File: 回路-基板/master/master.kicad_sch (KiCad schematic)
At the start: 28 parts, among them J1 Ext. PWR, J2 Conn_01x07_Pin, SW1 SW_SPDT, SW2 SW_SPDT, SW3 SW_SPDT, SW4 RESET, U1 TWE-L-DP-W, U2 LM1117MP-3.3, U3 DEV-16771

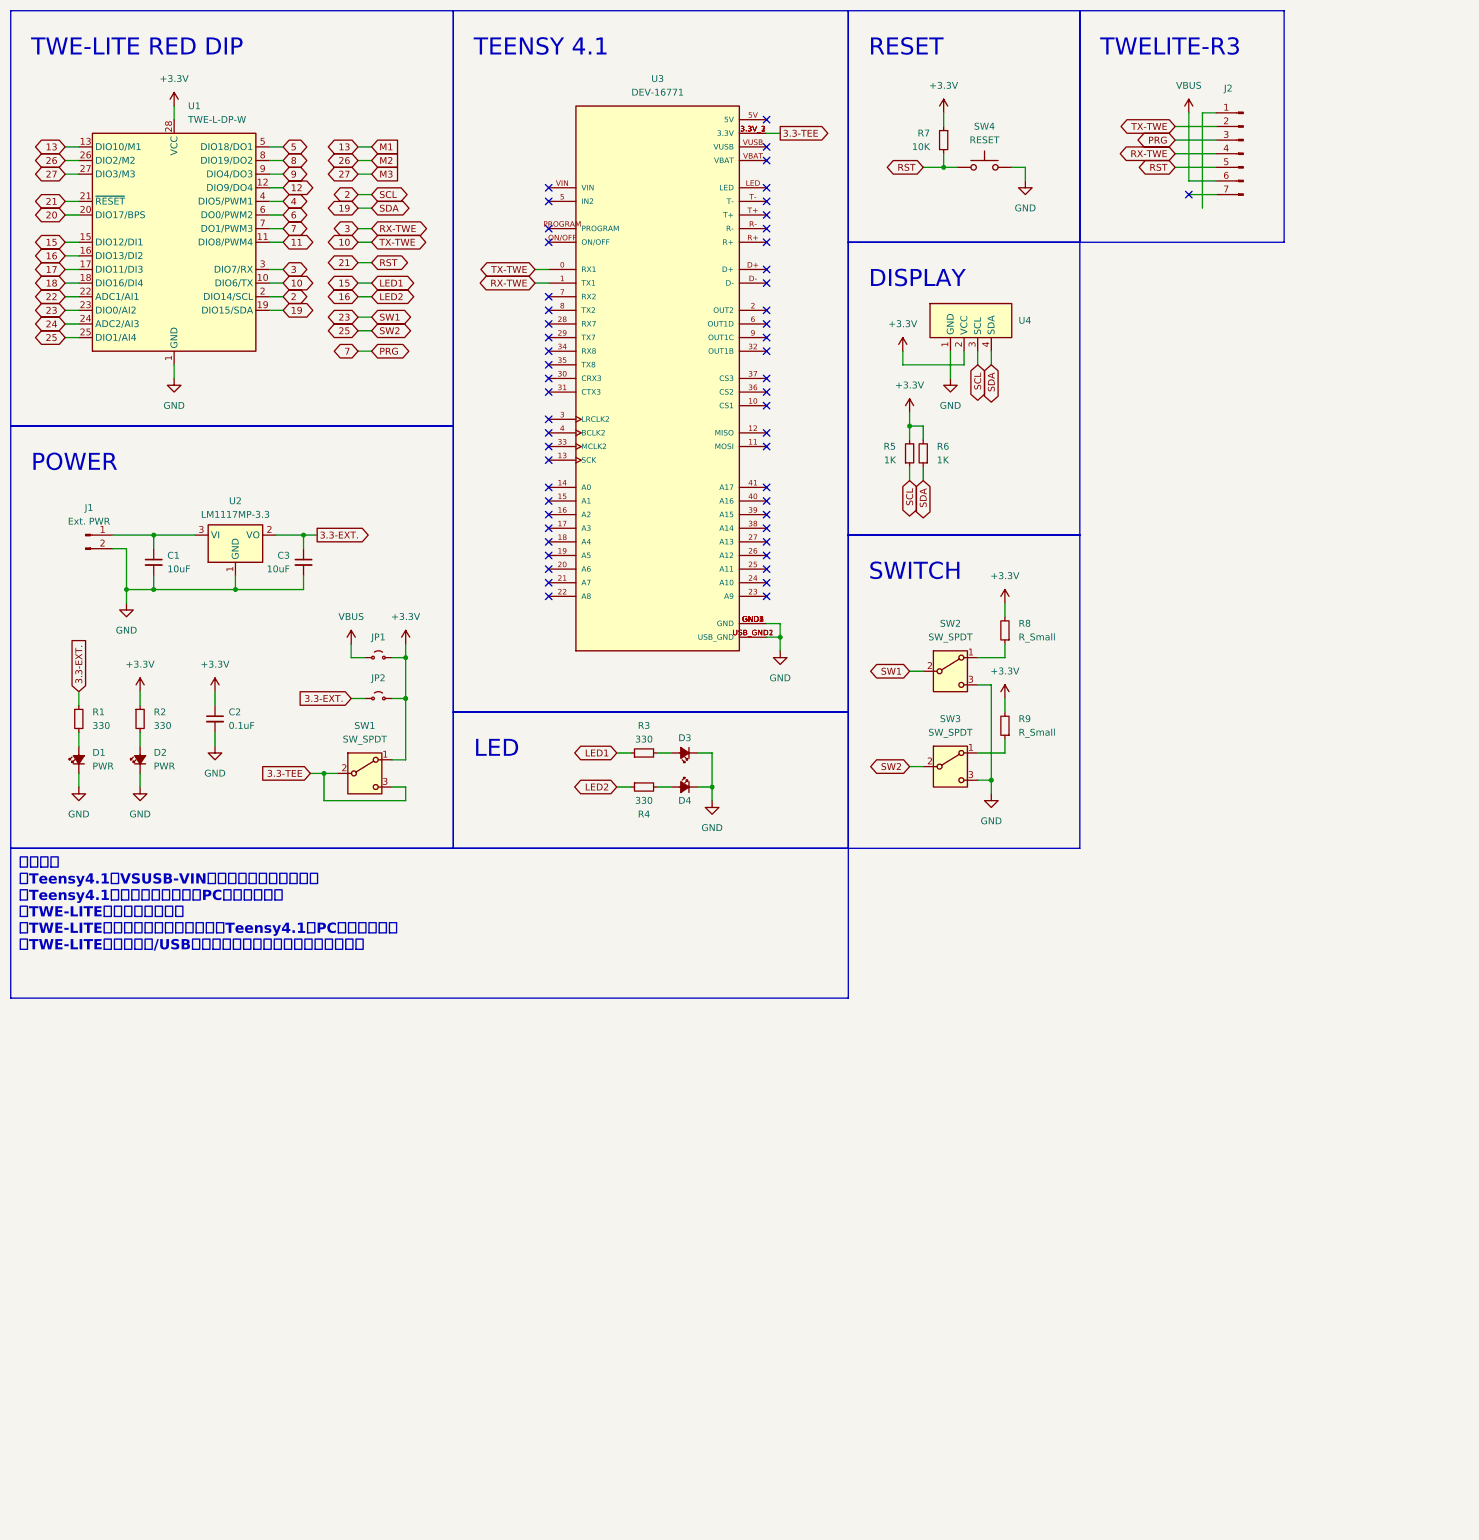
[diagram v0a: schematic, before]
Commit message: 親機基板のPCBを少し進めた
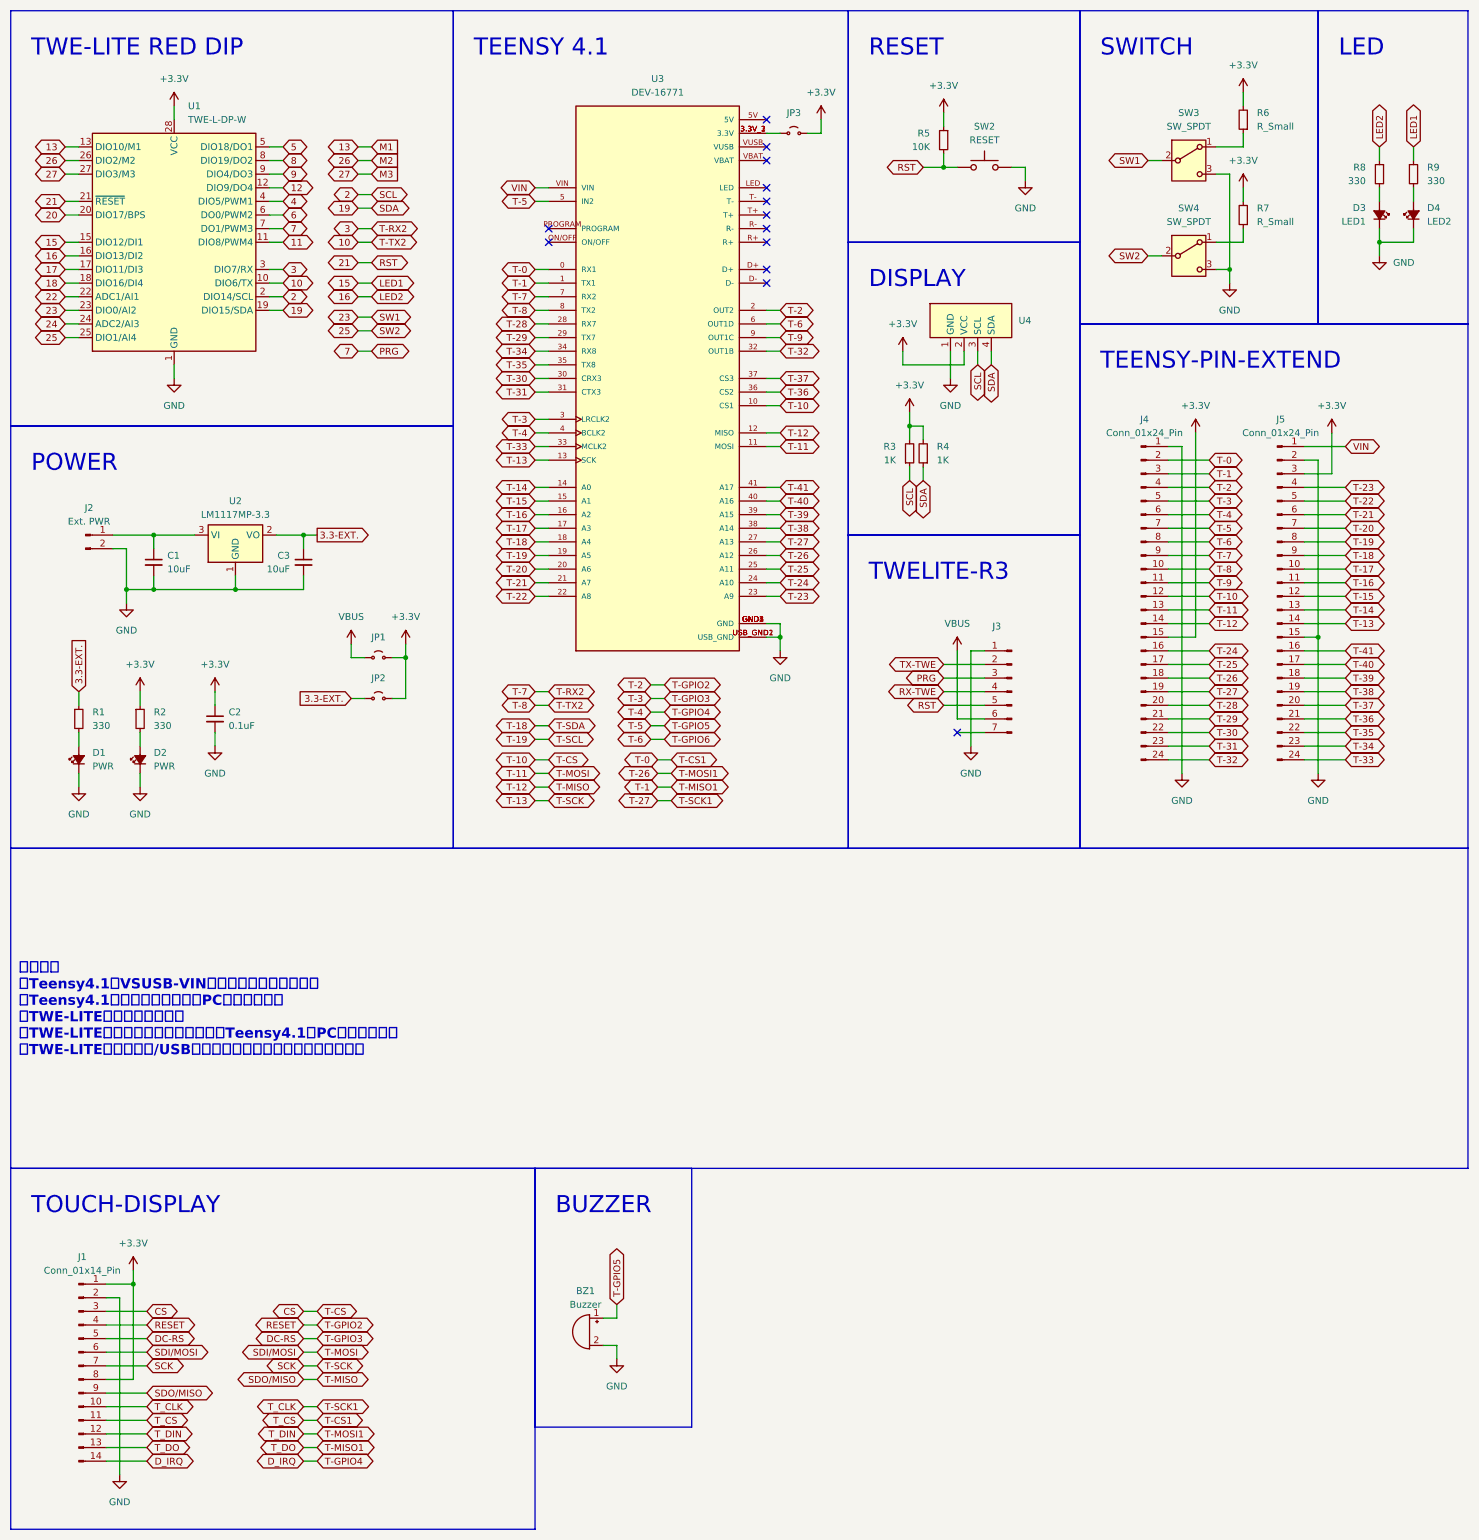
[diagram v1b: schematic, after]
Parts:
- removed R3, R4: 330, symbol Device:R_Small
- removed SW1: SW_SPDT, symbol Switch:SW_SPDT
- added BZ1: Buzzer, @2024-cansat:PKM13EPYH4000-A0, symbol Device:Buzzer
- added J1: Conn_01x14_Pin, Connector_PinSocket_2.54mm:PinSocket_1x14_P2.54mm_Vertical, symbol Connector:Conn_01x14_Pin
- added J4, J5: Conn_01x24_Pin, Connector_PinSocket_2.54mm:PinSocket_1x24_P2.54mm_Vertical, symbol Connector:Conn_01x24_Pin
- added JP3: Jumper_2_Small_Open, Jumper:SolderJumper-2_P1.3mm_Open_Pad1.0x1.5mm, symbol Jumper:Jumper_2_Small_Open
- added R8, R9: 330, Resistor_SMD:R_0603_1608Metric, symbol Device:R_Small
- C1, C2, C3: footprint (none) -> Capacitor_SMD:C_0603_1608Metric
- D1, D2, D3, D4: footprint (none) -> LED_SMD:LED_0805_2012Metric
- J2: renamed from J1; footprint (none) -> Connector_PinHeader_2.54mm:PinHeader_1x02_P2.54mm_Vertical
- J3: renamed from J2; footprint (none) -> Connector_PinSocket_2.54mm:PinSocket_1x07_P2.54mm_Vertical
- JP1, JP2: footprint (none) -> Jumper:SolderJumper-2_P1.3mm_Open_Pad1.0x1.5mm
- R1, R2: footprint (none) -> Resistor_SMD:R_0603_1608Metric
- R3: renamed from R5; footprint (none) -> Resistor_SMD:R_0603_1608Metric
- R4: renamed from R6; footprint (none) -> Resistor_SMD:R_0603_1608Metric
- R5: renamed from R7; footprint (none) -> Resistor_SMD:R_0603_1608Metric
- R6: renamed from R8; footprint (none) -> Resistor_SMD:R_0603_1608Metric
- R7: renamed from R9; footprint (none) -> Resistor_SMD:R_0603_1608Metric
- SW2: renamed from SW4; footprint (none) -> @2024-cansat:Tactile1
- SW3: renamed from SW2; footprint (none) -> @2024-cansat:SS12D01G4
- SW4: renamed from SW3; footprint (none) -> @2024-cansat:SS12D01G4
- U3: footprint DEV-16771:MODULE_DEV-16771 -> @2024-cansat:MODULE_DEV-16771
- U4: footprint (none) -> @2024-cansat:Display
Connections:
- net +3.3V: now also J1.1 (Pin_1), J1.8 (Pin_8), J4.15 (Pin_15), J5.3 (Pin_3), JP3.2 (B)
- net 10: now also U3.8 (TX2), J4.10 (Pin_10); no longer J3.2 (Pin_2), U3.0 (RX1)
- net 15: now also R9.1
- net 16: now also R8.1
- net 3: now also U3.7 (RX2), J4.9 (Pin_9); no longer J3.4 (Pin_4), U3.1 (TX1)
- net GND: now also J3.1 (Pin_1), BZ1.2 (-), J1.2 (Pin_2), J4.1 (Pin_1), J5.15 (Pin_15), J5.2 (Pin_2)
- net at D3.2 (A): now also R8.2
- net CS: now reaches U3.10 (CS1)
- net CS: now also J1.3 (Pin_3), J4.12 (Pin_12)
- net SDI/MOSI: now reaches U3.11 (MOSI)
- net SDI/MOSI: now also J1.6 (Pin_6), J4.13 (Pin_13)
- net SDO/MISO: now reaches U3.12 (MISO)
- net SDO/MISO: now also J1.9 (Pin_9), J4.14 (Pin_14)
- net SCK: now reaches U3.13 (SCK)
- net SCK: now also J1.7 (Pin_7), J5.14 (Pin_14)
- net T-14: now reaches U3.14 (A0)
- net T-14: now also J5.13 (Pin_13)
- net T-15: now reaches U3.15 (A1)
- net T-15: now also J5.12 (Pin_12)
- net T-16: now reaches U3.16 (A2)
- net T-16: now also J5.11 (Pin_11)
- net T-17: now reaches U3.17 (A3)
- net T-17: now also J5.10 (Pin_10)
- net T-18: now reaches U3.18 (A4)
- net T-18: now also J5.9 (Pin_9)
- net T-19: now reaches U3.19 (A5)
- net T-19: now also J5.8 (Pin_8)
- net RESET: now reaches U3.2 (OUT2)
- net RESET: now also J1.4 (Pin_4), J4.4 (Pin_4)
- net T-20: now reaches U3.20 (A6)
- net T-20: now also J5.7 (Pin_7)
- net T-21: now reaches U3.21 (A7)
- net T-21: now also J5.6 (Pin_6)
- net T-22: now reaches U3.22 (A8)
- net T-22: now also J5.5 (Pin_5)
- net T-23: now reaches U3.23 (A9)
- net T-23: now also J5.4 (Pin_4)
- net T-24: now reaches U3.24 (A10)
- net T-24: now also J4.16 (Pin_16)
- net T-25: now reaches U3.25 (A11)
- net T-25: now also J4.17 (Pin_17)
- net T-26: now reaches U3.26 (A12)
- net T-26: now also J1.12 (Pin_12), J4.18 (Pin_18)
- net T-27: now reaches U3.27 (A13)
- net T-27: now also J1.10 (Pin_10), J4.19 (Pin_19)
- net T-28: now reaches U3.28 (RX7)
- net T-28: now also J4.20 (Pin_20)
- net T-29: now reaches U3.29 (TX7)
- net T-29: now also J4.21 (Pin_21)
- net DC-RS: now reaches U3.3 (LRCLK2)
- net DC-RS: now also J1.5 (Pin_5), J4.5 (Pin_5)
- net T-30: now reaches U3.30 (CRX3)
- net T-30: now also J4.22 (Pin_22)
- net T-31: now reaches U3.31 (CTX3)
- net T-31: now also J4.23 (Pin_23)
- net T-32: now reaches U3.32 (OUT1B)
- net T-32: now also J4.24 (Pin_24)
- net T-33: now reaches U3.33 (MCLK2)
- net T-33: now also J5.24 (Pin_24)
- net T-34: now reaches U3.34 (RX8)
- net T-34: now also J5.23 (Pin_23)
- net T-35: now reaches U3.35 (TX8)
- net T-35: now also J5.22 (Pin_22)
- net T-36: now reaches U3.36 (CS2)
- net T-36: now also J5.21 (Pin_21)
- net T-37: now reaches U3.37 (CS3)
- net T-37: now also J5.20 (Pin_20)
- net T-38: now reaches U3.38 (A14)
- net T-38: now also J5.19 (Pin_19)
- net T-39: now reaches U3.39 (A15)
- net T-39: now also J5.18 (Pin_18)
- net D_IRQ: now reaches U3.4 (BCLK2)
- net D_IRQ: now also J1.14 (Pin_14), J4.6 (Pin_6)
- net T-40: now reaches U3.40 (A16)
- net T-40: now also J5.17 (Pin_17)
- net T-41: now reaches U3.41 (A17)
- net T-41: now also J5.16 (Pin_16)
- net T-5: now reaches U3.5 (IN2)
- net T-5: now also BZ1.1 (+), J4.7 (Pin_7)
- net T-6: now reaches U3.6 (OUT1D)
- net T-6: now also J4.8 (Pin_8)
- net T-9: now reaches U3.9 (OUT1C)
- net T-9: now also J4.11 (Pin_11)
- net VIN: now reaches U3.VIN
- net VIN: now also J5.1 (Pin_1)
- net at D4.2 (A): now also R9.2
- net 3.3-TEE: no longer names the net of U3.3.3V_1 (3.3V), U3.3.3V_2 (3.3V), U3.3.3V_3 (3.3V)
- net 3.3-TEE: now also JP3.1 (A)
- new net RX-TWE: J3.4 (Pin_4)
- new net T-0: J1.11 (Pin_11), J4.2 (Pin_2), U3.0 (RX1)
- new net T-1: J1.13 (Pin_13), J4.3 (Pin_3), U3.1 (TX1)
- new net TX-TWE: J3.2 (Pin_2)
- no-connect marks 54 -> 13
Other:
- note added: "BUZZER"
- note added: "TEENSY-PIN-EXTEND"
- note added: "TOUCH-DISPLAY"
- moved on the sheet: J3, R6, R7, SW3, SW4
